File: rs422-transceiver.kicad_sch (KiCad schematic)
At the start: 5 parts, among them J3 Conn_01x05_Pin, J4 Conn_01x06_Pin, U1 ADM3490ExR

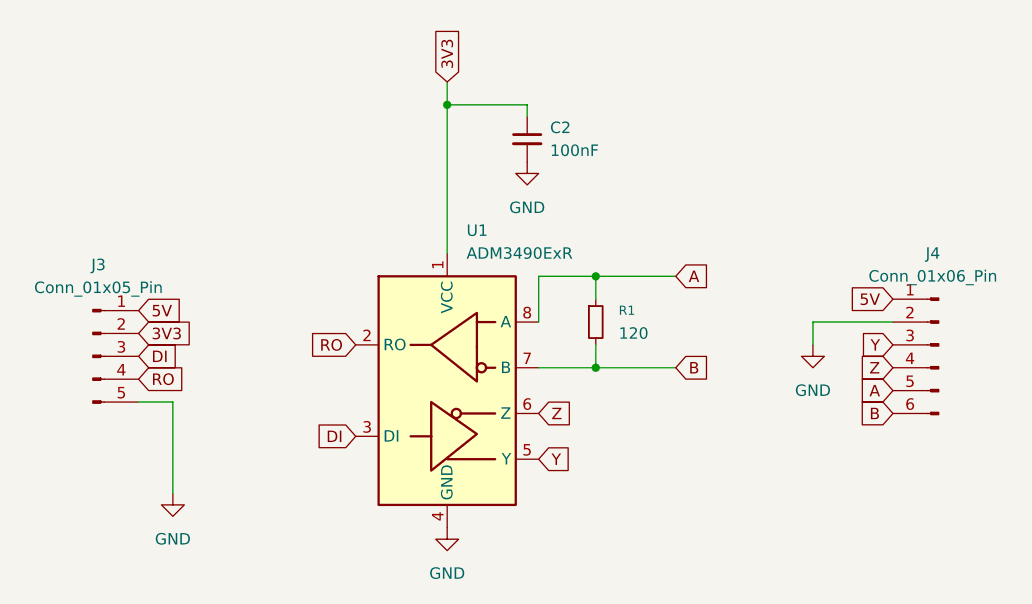
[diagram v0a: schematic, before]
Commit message: C2 -> C1
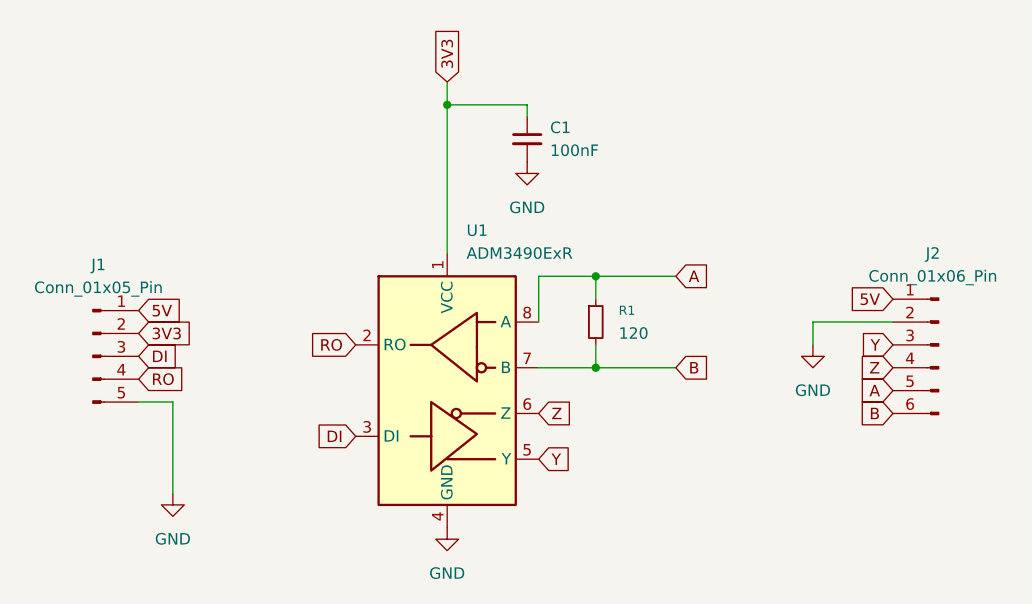
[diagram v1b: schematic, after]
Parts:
- renumbered C2 to C1, J3 to J1, J4 to J2
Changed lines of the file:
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@@
+		(dnp no)
+		(fields_autoplaced yes)
+		(property "Reference" "#PWR03"
+			(at 156.21 85.09 0)
+			(effects
+				(font
+					(size 1.27 1.27)
+				)
+				(hide yes)
+			)
+		)
+		(property "Value" "GND"
+			(at 156.21 83.82 0)
+			(effects
+				(font
+					(size 1.27 1.27)
+				)
+			)
+		)
+		(property "Footprint" ""
+			(at 156.21 78.74 0)
+			(effects
+				(font
+					(size 1.27 1.27)
+				)
+				(hide yes)
+			)
+		)
+		(property "Datasheet" ""
+			(at 156.21 78.74 0)
+			(effects
+				(font
+					(size 1.27 1.27)
+				)
+				(hide yes)
+			)
+		)
+		(property "Description" "Power symbol creates a global label with name \"GND\" , ground"
+			(at 156.21 78.74 0)
+			(effects
+				(font
+					(size 1.27 1.27)
+				)
+				(hide yes)
+			)
+		)
+		(pin "1"
+		)
+		(instances
+			(project "rs422-transceiver"
+				(path "/9a069c72-07e2-4a46-b768-1a075e2ff1d8"
+					(reference "#PWR03")
+					(unit 1)
+				)
+			)
+		)
+	)
+	(symbol
+		(lib_id "power:GND")
+		(at 187.96 99.06 0)
+		(unit 1)
+		(exclude_from_sim no)
+		(in_bom yes)
+		(on_board yes)
 		(dnp no)
 		(fields_autoplaced yes)
 		(property "Reference" "#PWR04"
-			(at 156.21 85.09 0)
-			(effects
-				(font
-					(size 1.27 1.27)
-				)
-				(hide yes)
-			)
-		)
-		(property "Value" "GND"
-			(at 156.21 83.82 0)
-			(effects
-				(font
-					(size 1.27 1.27)
-				)
-			)
-		)
-		(property "Footprint" ""
-			(at 156.21 78.74 0)
-			(effects
-				(font
-					(size 1.27 1.27)
-				)
-				(hide yes)
-			)
-		)
-		(property "Datasheet" ""
-			(at 156.21 78.74 0)
-			(effects
-				(font
-					(size 1.27 1.27)
-				)
-				(hide yes)
-			)
-		)
-		(property "Description" "Power symbol creates a global label with name \"GND\" , ground"
-			(at 156.21 78.74 0)
-			(effects
-				(font
-					(size 1.27 1.27)
-				)
-				(hide yes)
-			)
-		)
-		(pin "1"
-		)
-		(instances
-			(project "rs422-transceiver"
-				(path "/9a069c72-07e2-4a46-b768-1a075e2ff1d8"
-					(reference "#PWR04")
-					(unit 1)
-				)
-			)
-		)
-	)
-	(symbol
-		(lib_id "power:GND")
-		(at 187.96 99.06 0)
-		(unit 1)
-		(exclude_from_sim no)
-		(in_bom yes)
-		(on_board yes)
-		(dnp no)
-		(fields_autoplaced yes)
-		(property "Reference" "#PWR03"
 			(at 187.96 105.41 0)
 			(effects
@@
 			(project "rs422-transceiver"
 				(path "/9a069c72-07e2-4a46-b768-1a075e2ff1d8"
-					(reference "#PWR03")
+					(reference "#PWR04")
 					(unit 1)
 				)
@@
 		(on_board yes)
 		(dnp no)
-		(property "Reference" "J4"
+		(property "Reference" "J2"
 			(at 201.295 88.9 0)
 			(effects
@@
 			(project ""
 				(path "/9a069c72-07e2-4a46-b768-1a075e2ff1d8"
-					(reference "J4")
+					(reference "J2")
 					(unit 1)
 				)
@@
 		(dnp no)
 		(fields_autoplaced yes)
-		(property "Reference" "C2"
+		(property "Reference" "C1"
 			(at 158.75 74.9362 0)
 			(effects
@@
 			(project ""
 				(path "/9a069c72-07e2-4a46-b768-1a075e2ff1d8"
-					(reference "C2")
+					(reference "C1")
 					(unit 1)
 				)
@@
 		(on_board yes)
 		(dnp no)
-		(property "Reference" "J3"
+		(property "Reference" "J1"
 			(at 108.585 90.17 0)
 			(effects
@@
 			(project ""
 				(path "/9a069c72-07e2-4a46-b768-1a075e2ff1d8"
-					(reference "J3")
-					(unit 1)
-				)
+					(reference "J1")
+					(unit 1)
+				)
